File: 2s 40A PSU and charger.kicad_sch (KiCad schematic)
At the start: 5 parts

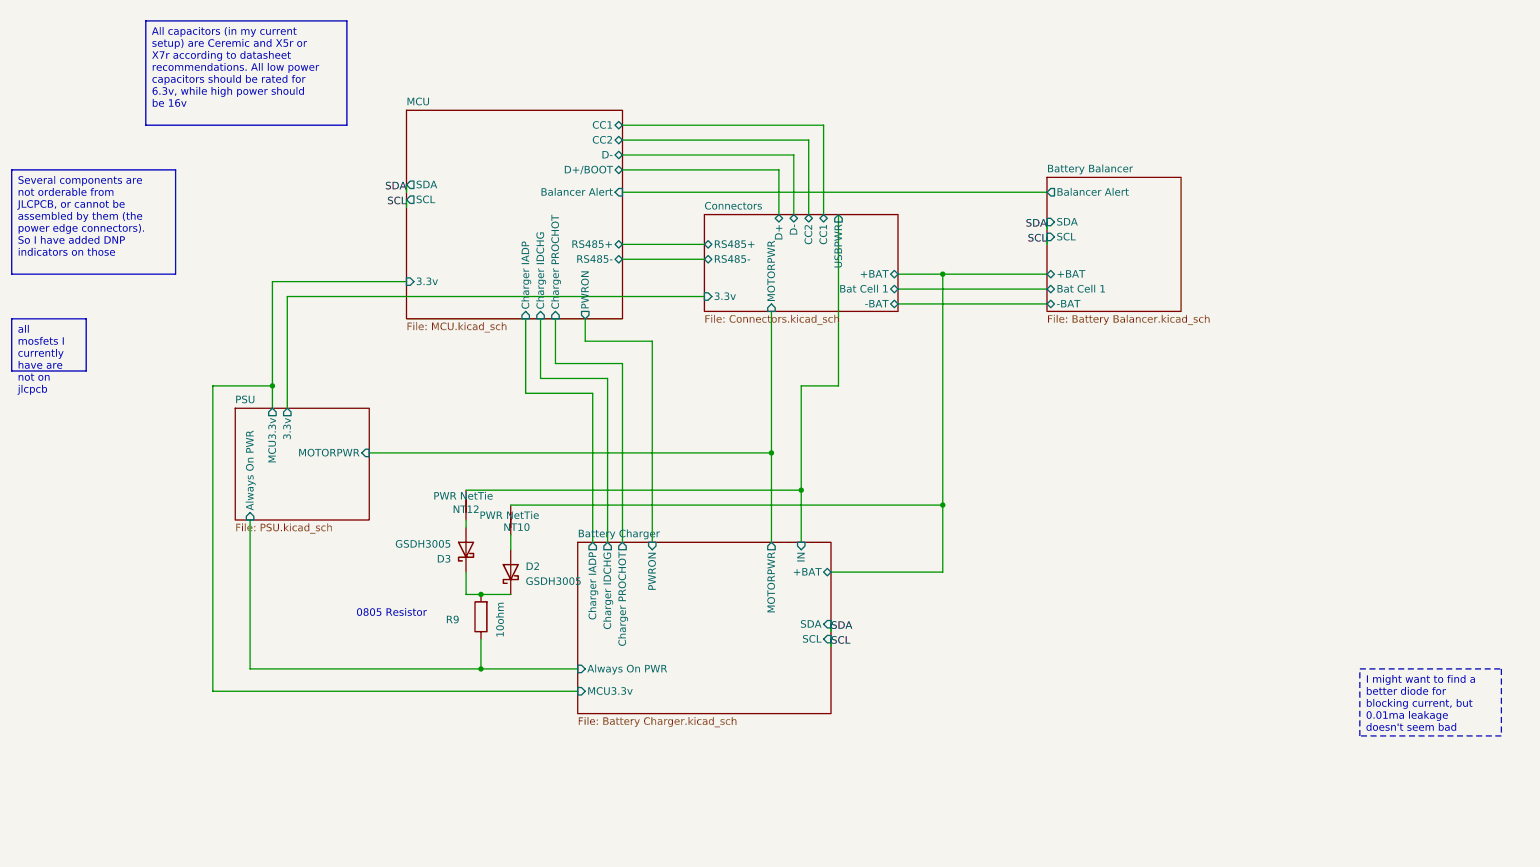
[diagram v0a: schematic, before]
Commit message: Clarified top level schematic
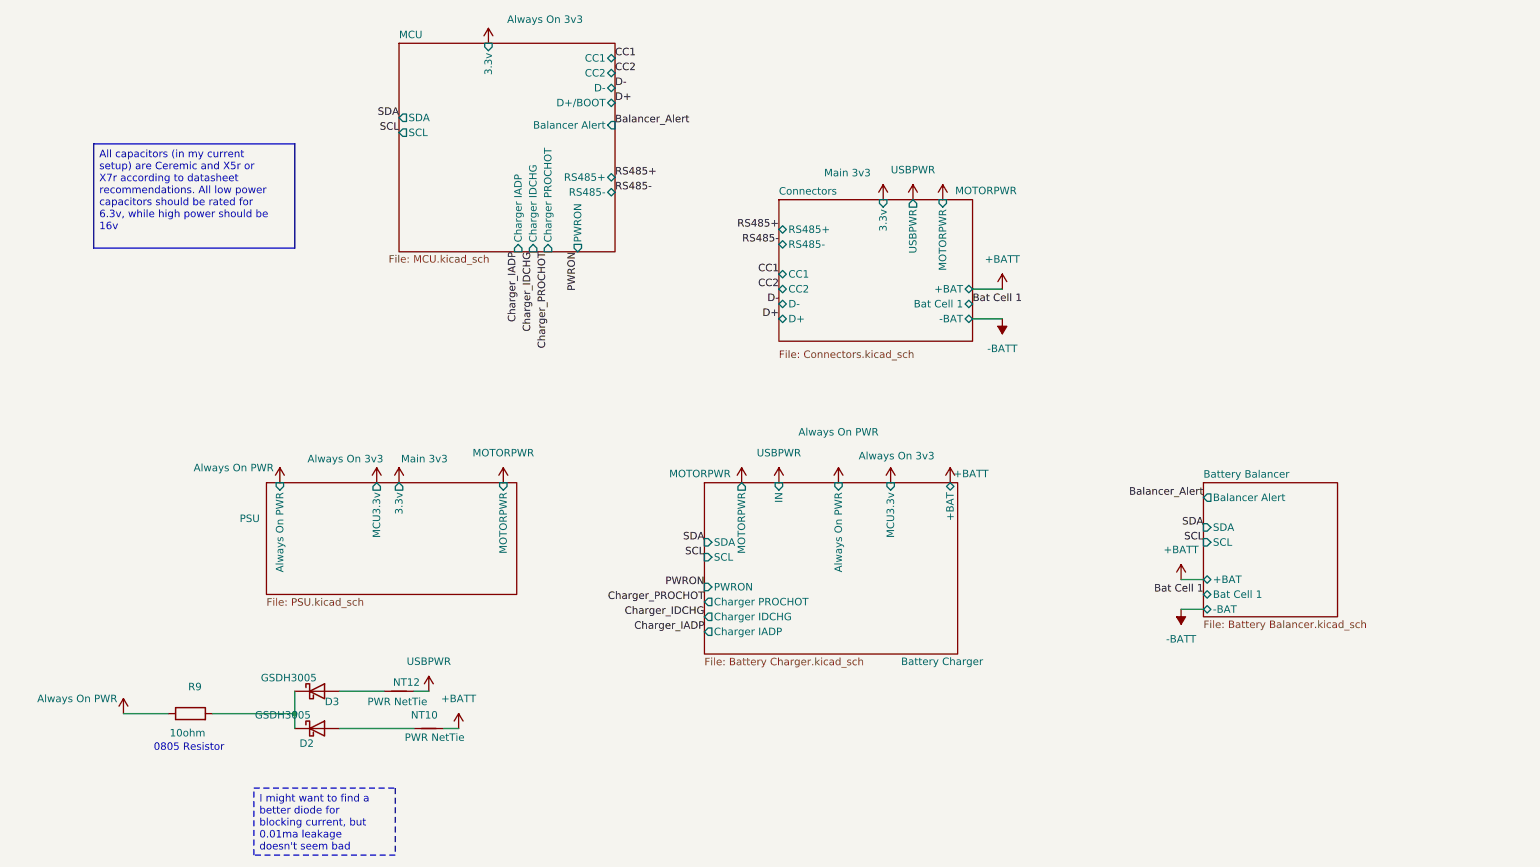
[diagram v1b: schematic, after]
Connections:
- net Battery Balancer/+BAT renamed +BATT
- net Battery Charger/Always On PWR renamed Always On PWR
- net Battery Charger/IN renamed USBPWR
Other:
- moved on the sheet: D2, D3, NT10, NT12, R9

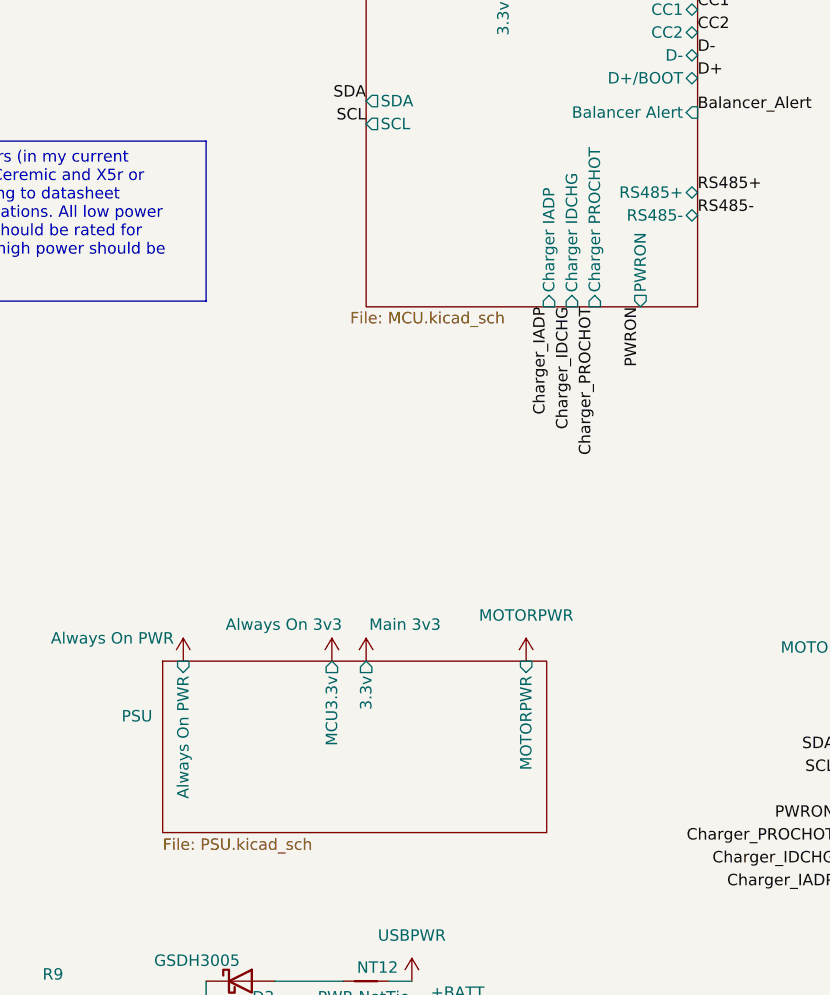
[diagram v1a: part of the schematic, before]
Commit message: Added MCU boot button, 3v3 power enable, and pulldown on adaptor enable
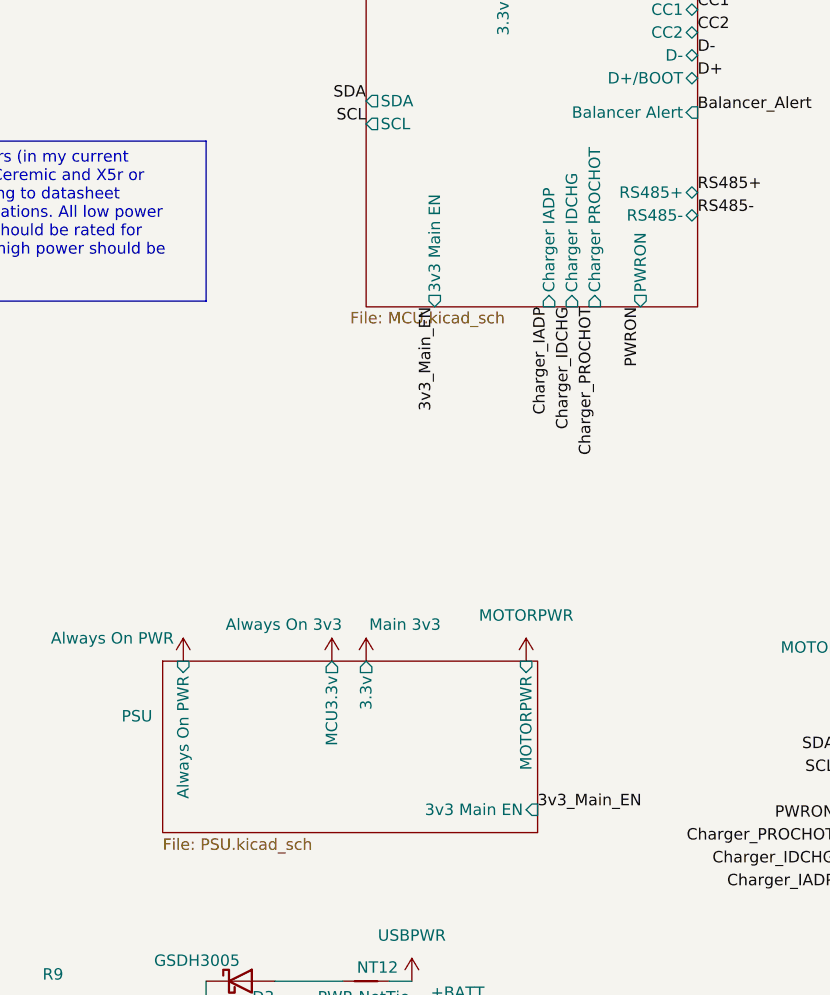
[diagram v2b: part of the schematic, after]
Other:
- sheet MCU ports: added 3v3 Main EN; removed none
- sheet PSU ports: added 3v3 Main EN; removed none
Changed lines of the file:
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@@
+		)
+	)
+	(label "3v3_Main_EN"
+		(at 104.14 76.2 270)
+		(effects
+			(font
+				(size 1.27 1.27)
+			)
+			(justify right bottom)
 		)
 	)
@@
 	(label "RS485+"
 		(at 133.35 63.5 0)
+		(effects
+			(font
+				(size 1.27 1.27)
+			)
+			(justify left bottom)
+		)
+	)
+	(label "3v3_Main_EN"
+		(at 115.57 132.08 0)
 		(effects
 			(font
@@
 			)
 		)
+		(pin "3v3 Main EN" output
+			(at 104.14 76.2 270)
+			(effects
+				(font
+					(size 1.27 1.27)
+				)
+				(justify left)
+			)
+		)
 		(instances
 			(project "2s 40A PSU and charger"
@@
 	(sheet
 		(at 73.914 115.57)
-		(size 42.672 19.05)
+		(size 41.656 19.05)
 		(exclude_from_sim no)
 		(in_bom yes)
@@
 			(effects
 				(font
+					(size 1.27 1.27)
+				)
+				(justify right)
+			)
+		)
+		(pin "3v3 Main EN" input
+			(at 115.57 132.08 0)
+			(effects
+				(font
